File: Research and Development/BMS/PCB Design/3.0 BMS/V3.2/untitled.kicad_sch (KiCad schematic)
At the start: 15 parts, among them J2 Charger out, J3 PWR IN, Q2 PN100, SW2 ctrl view sw, U9 L78L05_SOT89

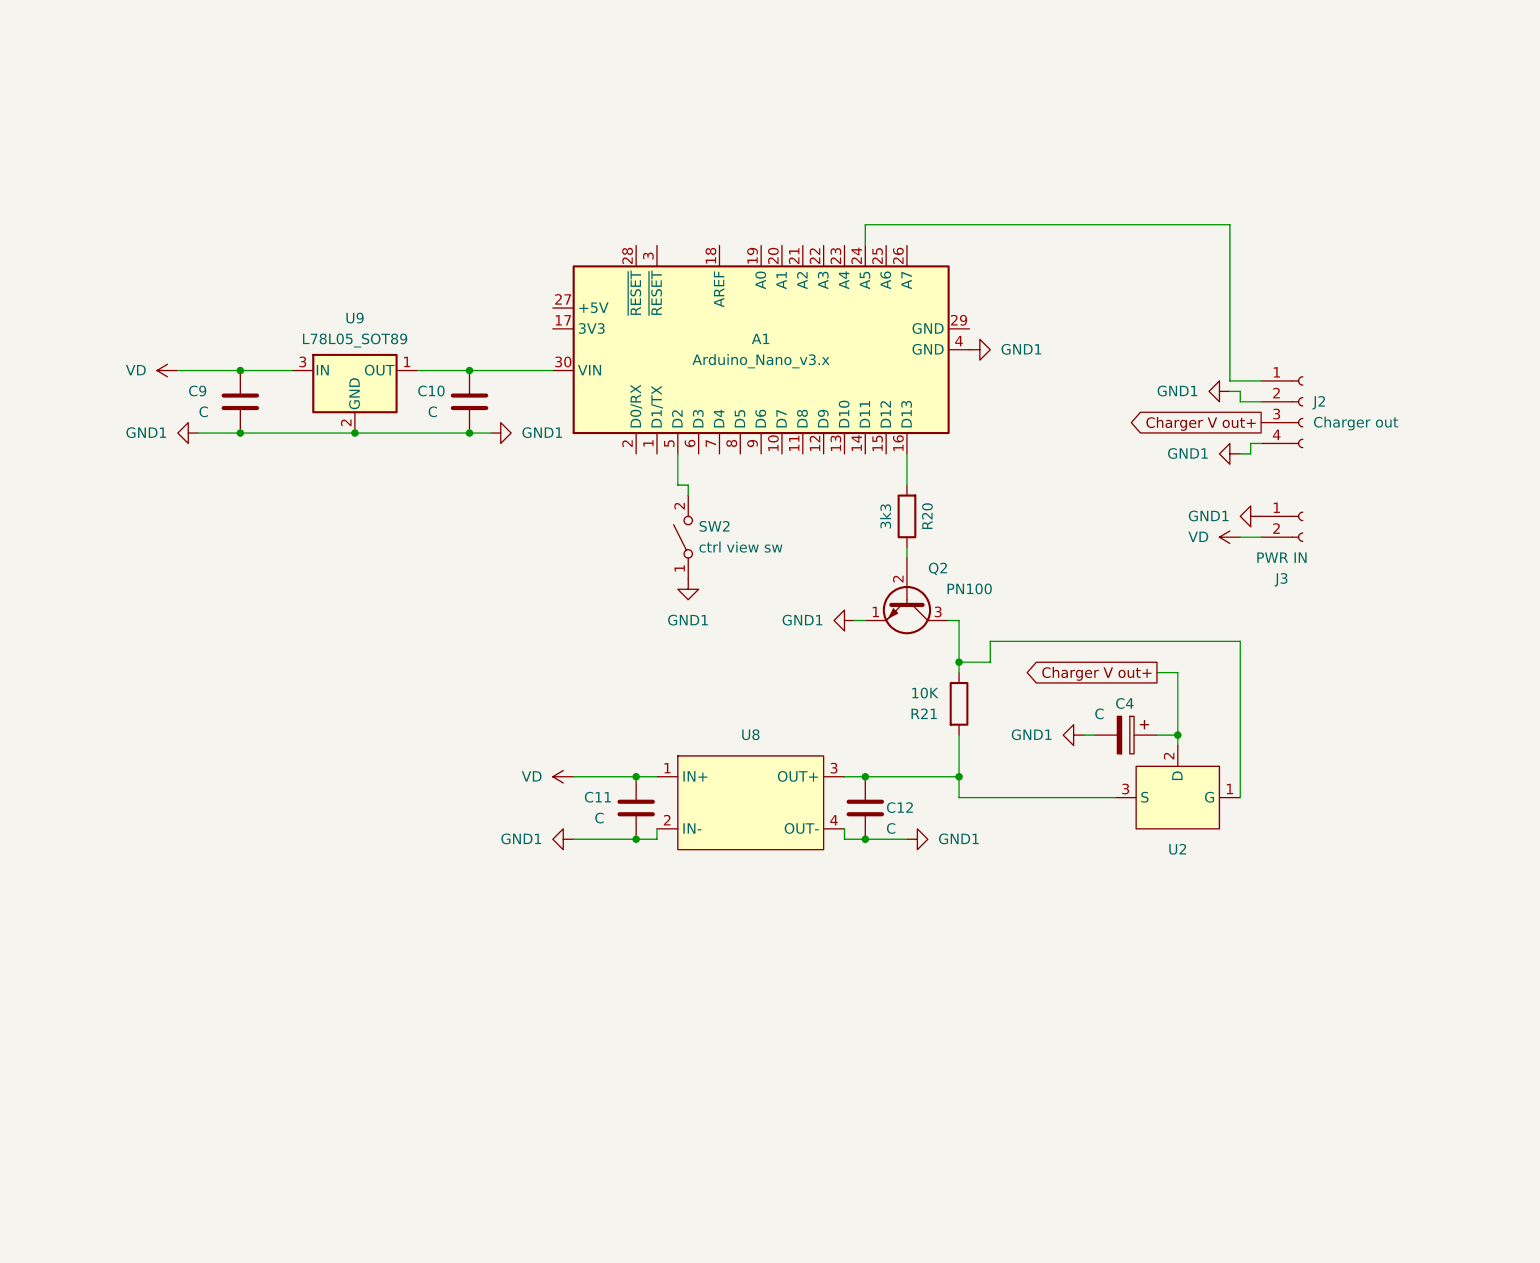
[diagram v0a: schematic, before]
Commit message: updated bms schem
fixed polarity on batteries, updated jst conns to XH, created footprints for them, tidied up and shrunk the board size, changed from using the ds18d20b to a 10k ntc thermistor for temperature control protection
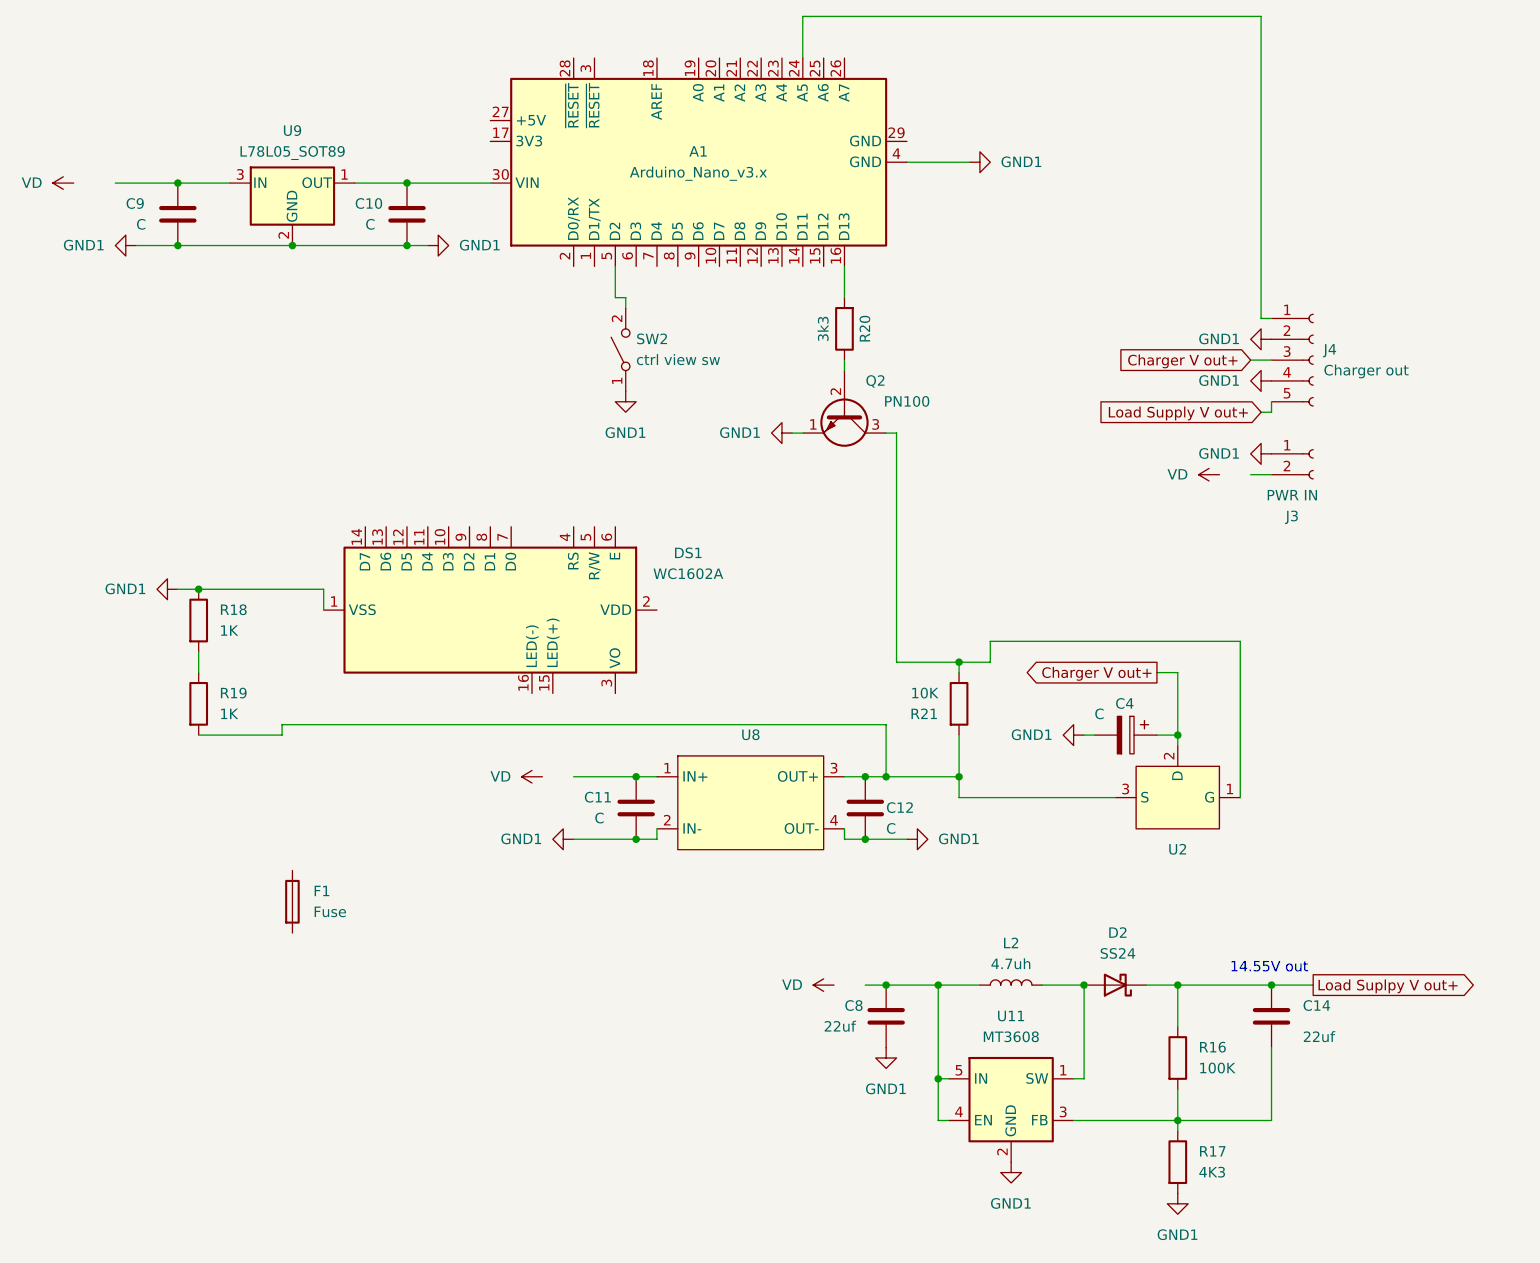
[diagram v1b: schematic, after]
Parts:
- removed J2: Charger out, Connector_JST:JST_GH_SM04B-GHS-TB_1x04-1MP_P1.25mm_Horizontal, symbol Connector:Conn_01x04_Socket
- added C14, C8: 22uf, symbol Device:C
- added D2: SS24, symbol Device:D_Schottky
- added DS1: WC1602A, Display:WC1602A, symbol Display_Character:WC1602A
- added F1: Fuse, symbol Device:Fuse
- added J4: Charger out, symbol Connector:Conn_01x05_Socket
- added L2: 4.7uh, symbol Device:L
- added R16: 100K, symbol Device:R
- added R17: 4K3, symbol Device:R
- added R18, R19: 1K, symbol Device:R
- added U11: MT3608, Package_TO_SOT_SMD:SOT-23-6, symbol Regulator_Switching:MT3608
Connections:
- net Charger V out+: now also J4.3 (Pin_3)
- net GND1: now also C8.2, DS1.1 (VSS), J4.2 (Pin_2), J4.4 (Pin_4), R17.2, R18.1, U11.2 (GND)
- net VD: no longer C11.2, C9.2, J3.2 (Pin_2), U8.1 (IN+), U9.3 (IN)
- net at A1.24 (A5): now also J4.1 (Pin_1)
- net at C12.2, R21.2, U2.3 (S)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: now also R19.2
- new net: C8.1, L2.1, U11.4 (EN), U11.5 (IN)
- new net: D2.2 (A), L2.2, U11.1 (SW)
- new net: C9.2, U9.3 (IN)
- new net: C14.2, R16.2, R17.1, U11.3 (FB)
- new net: C11.2, U8.1 (IN+)
- new net: R18.2, R19.1
- new net Load Suplpy V out+: C14.1, D2.1 (K), R16.1
- new net Load Supply V out+: J4.5 (Pin_5)
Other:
- note added: "14.55V out"
- moved on the sheet: A1, C10, C9, J3, Q2, R20, SW2, U9

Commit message: redone bms board and added test bms schem and board to test functionality without the batteries
added:
- bms test schem and layout
- updated bms
- testing of quad rotary encoder breakout board
- testing of teensy audio board
- combining the encoders and audio board in 1 circuit with limited control of chorus fx with encoders
- created text based skeleton structure of GUI of the interface with use of encoders and home button
- created file for adding fx functionality. will be now incorperating fx
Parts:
- removed A1: Arduino_Nano_v3.x, Module:Arduino_Nano, symbol MCU_Module:Arduino_Nano_v3.x
- removed C10, C11, C12, C9: C, symbol Device:C
- removed C14, C8: 22uf, symbol Device:C
- removed C4: C, symbol Device:C_Polarized
- removed D2: SS24, symbol Device:D_Schottky
- removed DS1: WC1602A, Display:WC1602A, symbol Display_Character:WC1602A
- removed F1: Fuse, symbol Device:Fuse
- removed J3: PWR IN, Connector_JST:JST_GH_SM02B-GHS-TB_1x02-1MP_P1.25mm_Horizontal, symbol Connector:Conn_01x02_Socket
- removed J4: Charger out, symbol Connector:Conn_01x05_Socket
- removed L2: 4.7uh, symbol Device:L
- removed Q2: PN100, Package_TO_SOT_SMD:SOT-23, symbol Transistor_BJT:PN2222A
- removed R16: 100K, symbol Device:R
- removed R17: 4K3, symbol Device:R
- removed R18, R19: 1K, symbol Device:R
- removed R20: 3k3, Resistor_SMD:R_1206_3216Metric, symbol Device:R
- removed R21: 10K, Resistor_SMD:R_1206_3216Metric, symbol Device:R
- removed SW2: ctrl view sw, symbol Switch:SW_SPST
- removed U11: MT3608, Package_TO_SOT_SMD:SOT-23-6, symbol Regulator_Switching:MT3608
- removed U2: ~, Package_TO_SOT_SMD:TO-252-2, symbol BMS-MK2-symbols:AOD409
- removed U8: ~, symbol chargersymbols:DCDC_CHG_CONV
- removed U9: L78L05_SOT89, Package_TO_SOT_SMD:SOT-89-3, symbol Regulator_Linear:L78L05_SOT89
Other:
- note removed: "14.55V out"
